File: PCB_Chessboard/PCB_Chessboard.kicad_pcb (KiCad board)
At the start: 4 copper layers, 200 x 200 mm, 75 parts, among them J10 Conn_01x02, J11 Conn_01x02, J12 Conn_01x02, J13 Conn_01x02, J14 Conn_01x02, J15 Conn_01x02, J16 Conn_01x02, J17 Conn_01x02, J18 Conn_01x02, J19 Conn_01x03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

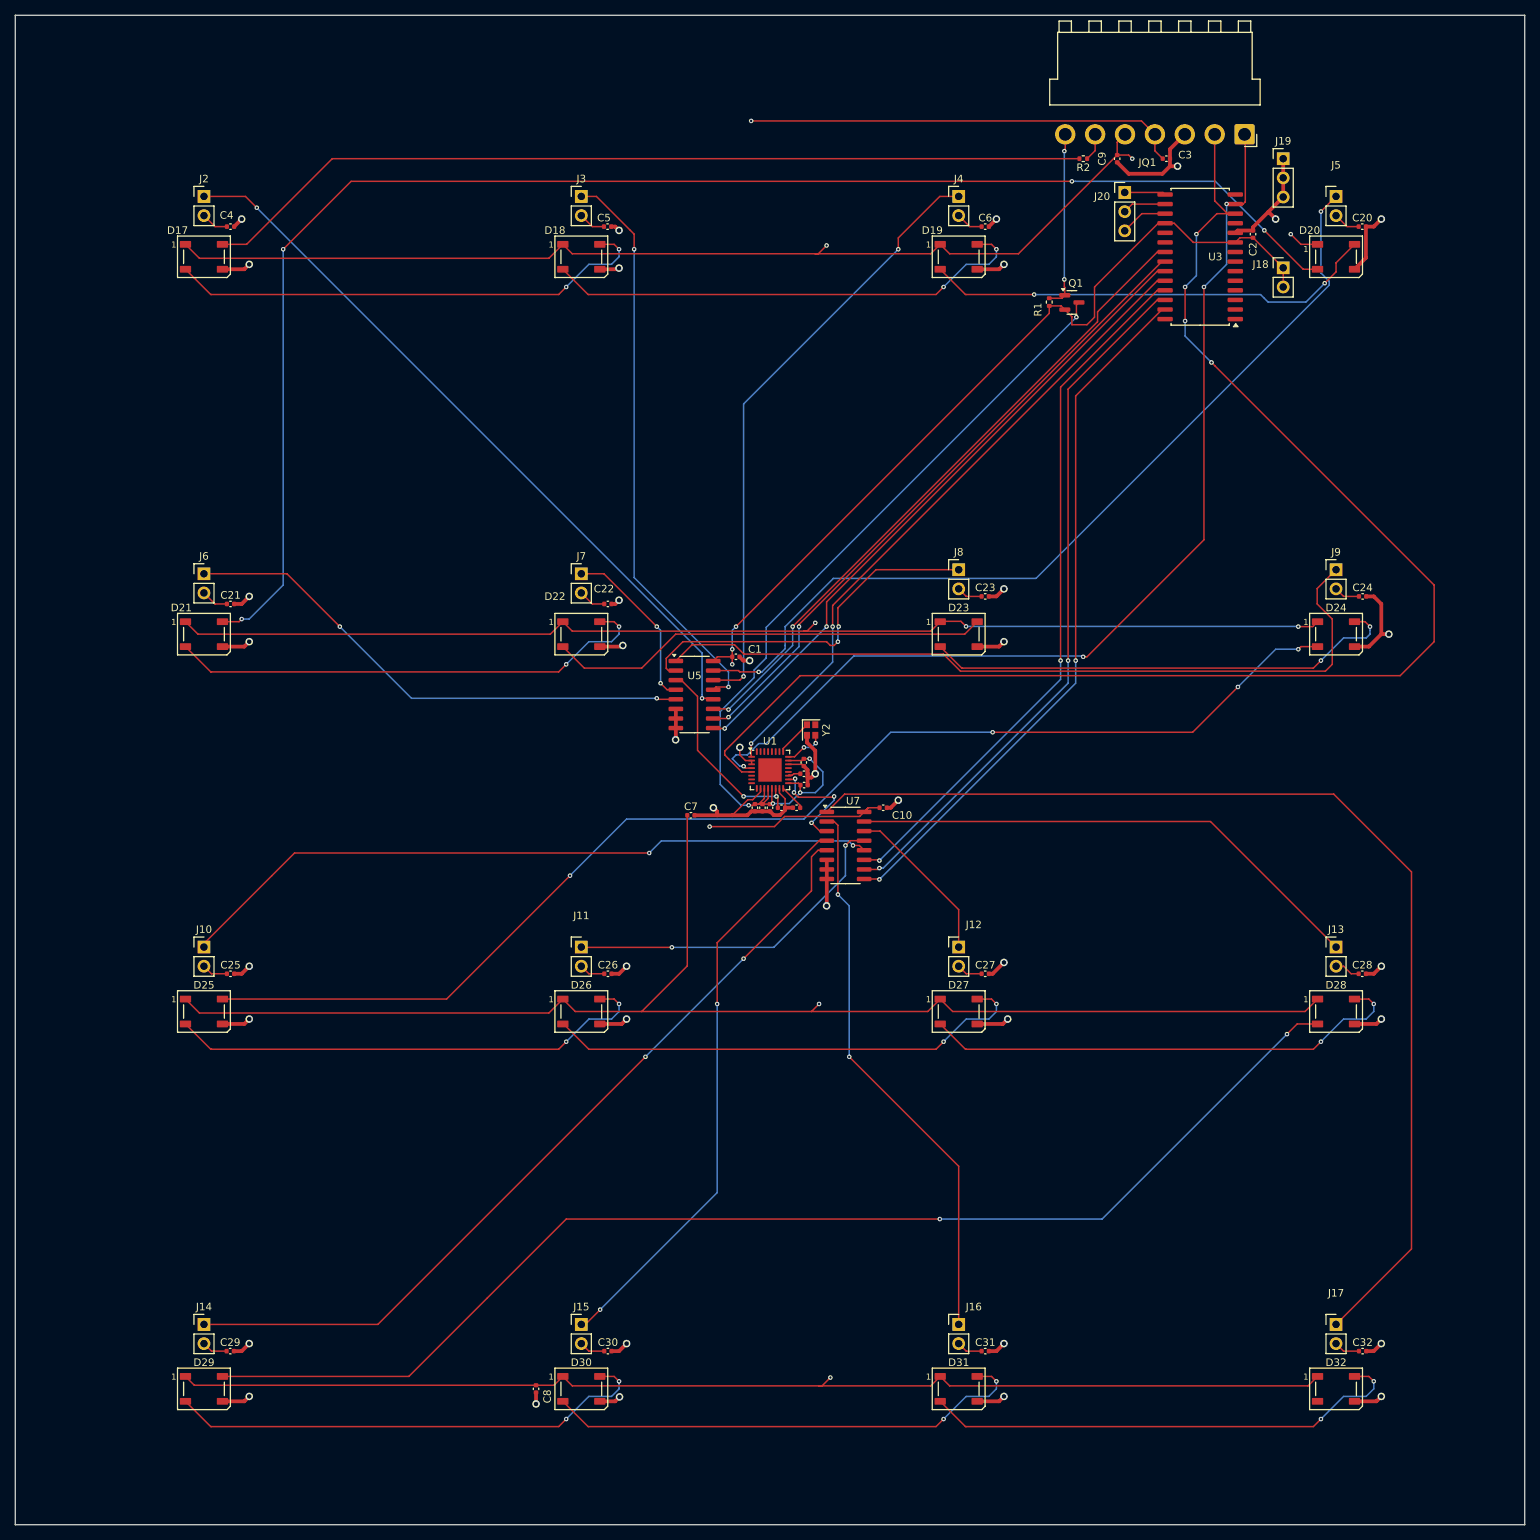
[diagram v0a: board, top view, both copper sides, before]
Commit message: PCB quadrant with mounting Hole
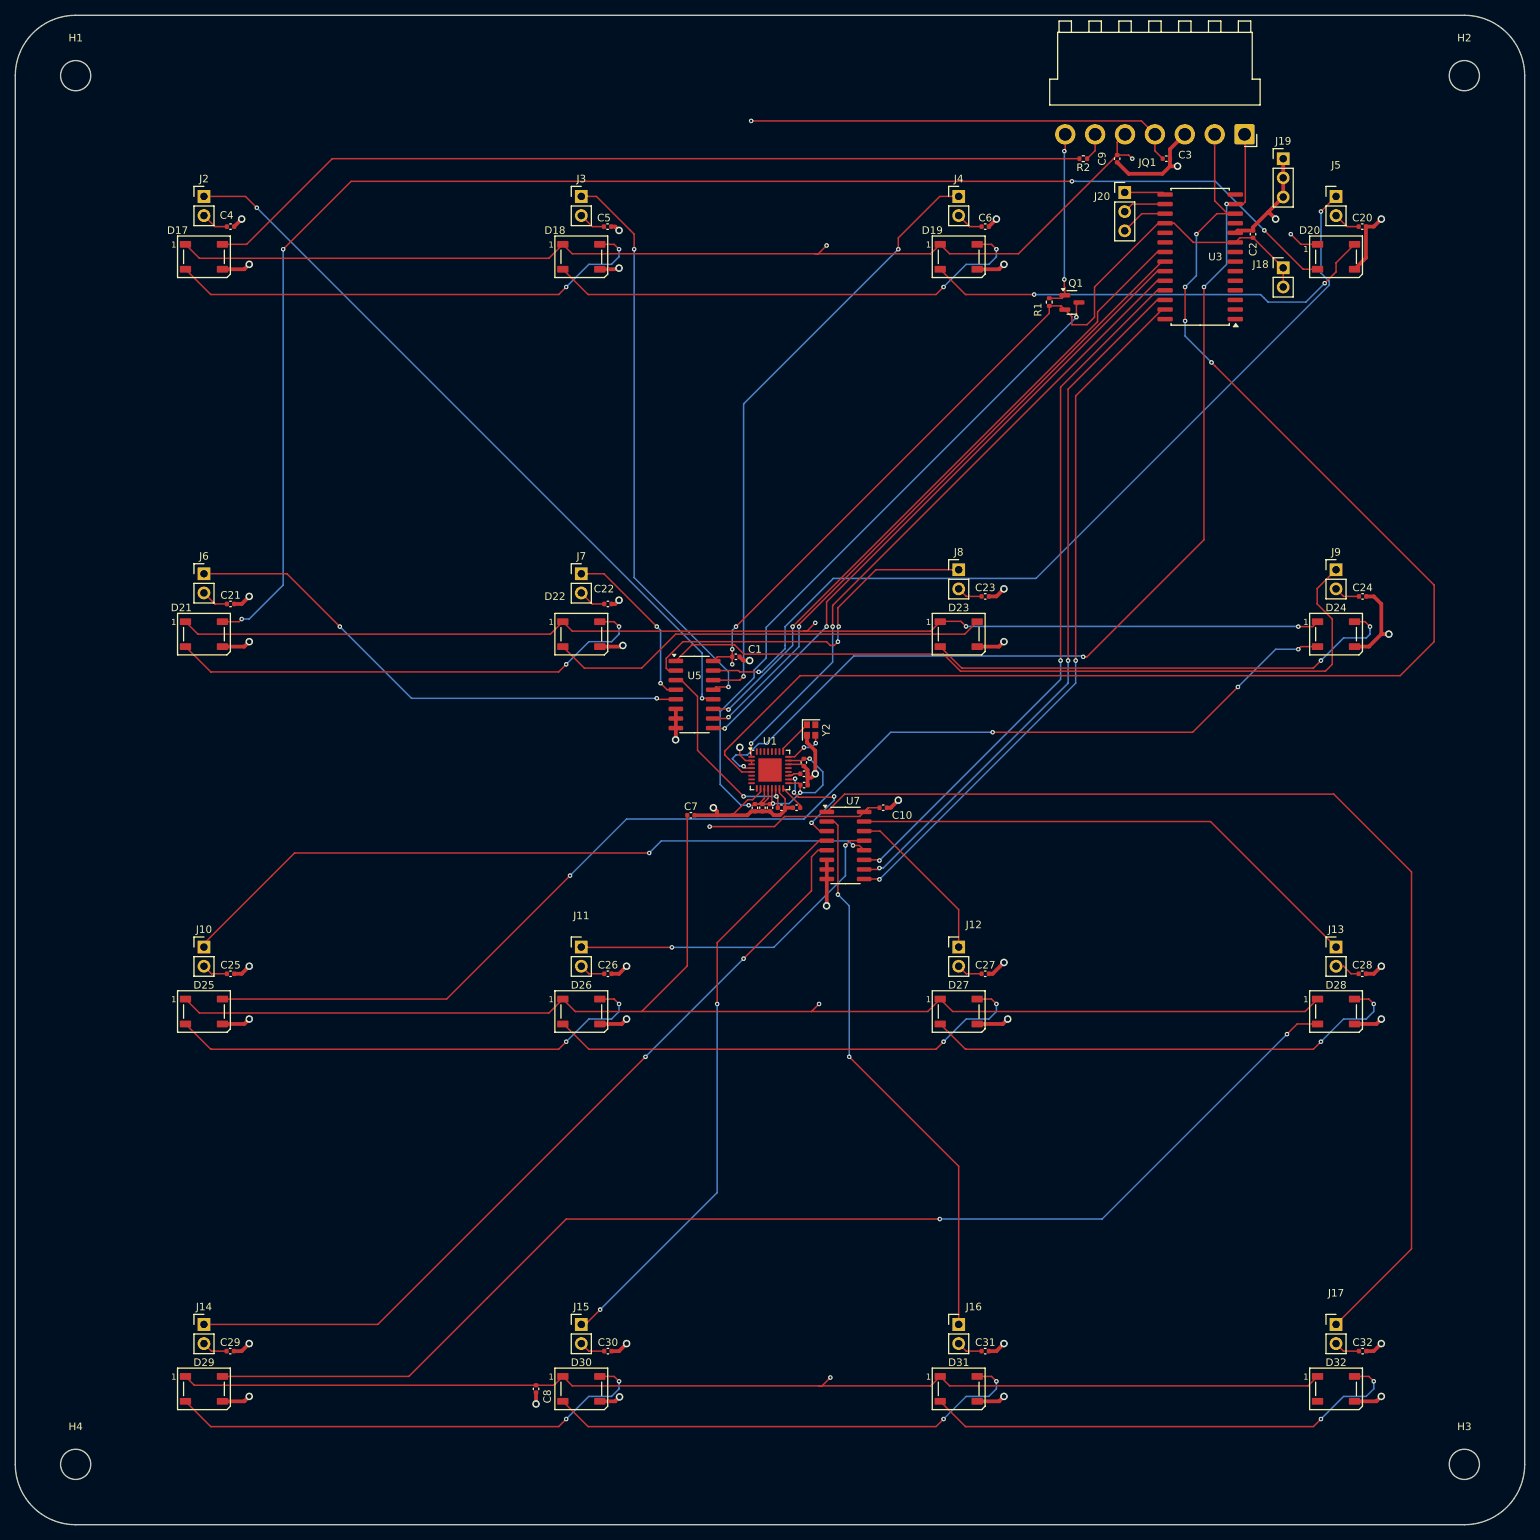
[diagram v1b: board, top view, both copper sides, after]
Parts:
- added H1: MountingHole, MountingHole:MountingHole_4mm, F.Cu at (8.00, 8.00)
- added H2: MountingHole, MountingHole:MountingHole_4mm, F.Cu at (192.0, 8.00)
- added H3: MountingHole, MountingHole:MountingHole_4mm, F.Cu at (192.0, 192.0)
- added H4: MountingHole, MountingHole:MountingHole_4mm, F.Cu at (8.00, 192.0)
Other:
- outline, holes or cut-outs redrawn
